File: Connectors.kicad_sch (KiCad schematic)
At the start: 23 parts, among them J1 Precidip 853-87-004-20-001101, J10 Precidip 853-87-004-20-001101, J11 7 pin FPC 0.3mm Aces 51688-00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, J12 Precidip 853-87-004-20-001101, J13 TE 3-2363961-0 receptacle, J15 Precidip 853-87-004-20-001101, J16 TE 3-2363961-0 receptacle, J18 Precidip 852-10-004-20-001101, J2 Precidip 853-87-004-20-001101, J3 7 pin FPC 0.3mm Aces 51688-00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, J4 Precidip 853-87-004-20-001101, J5 7 pin FPC 0.3mm Aces 51688-00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, J6 Precidip 853-87-004-20-001101, J7 Precidip 853-87-004-20-001101, J8 7 pin FPC 0.3mm Aces 51688-00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, J9 Precidip 853-87-004-20-001101

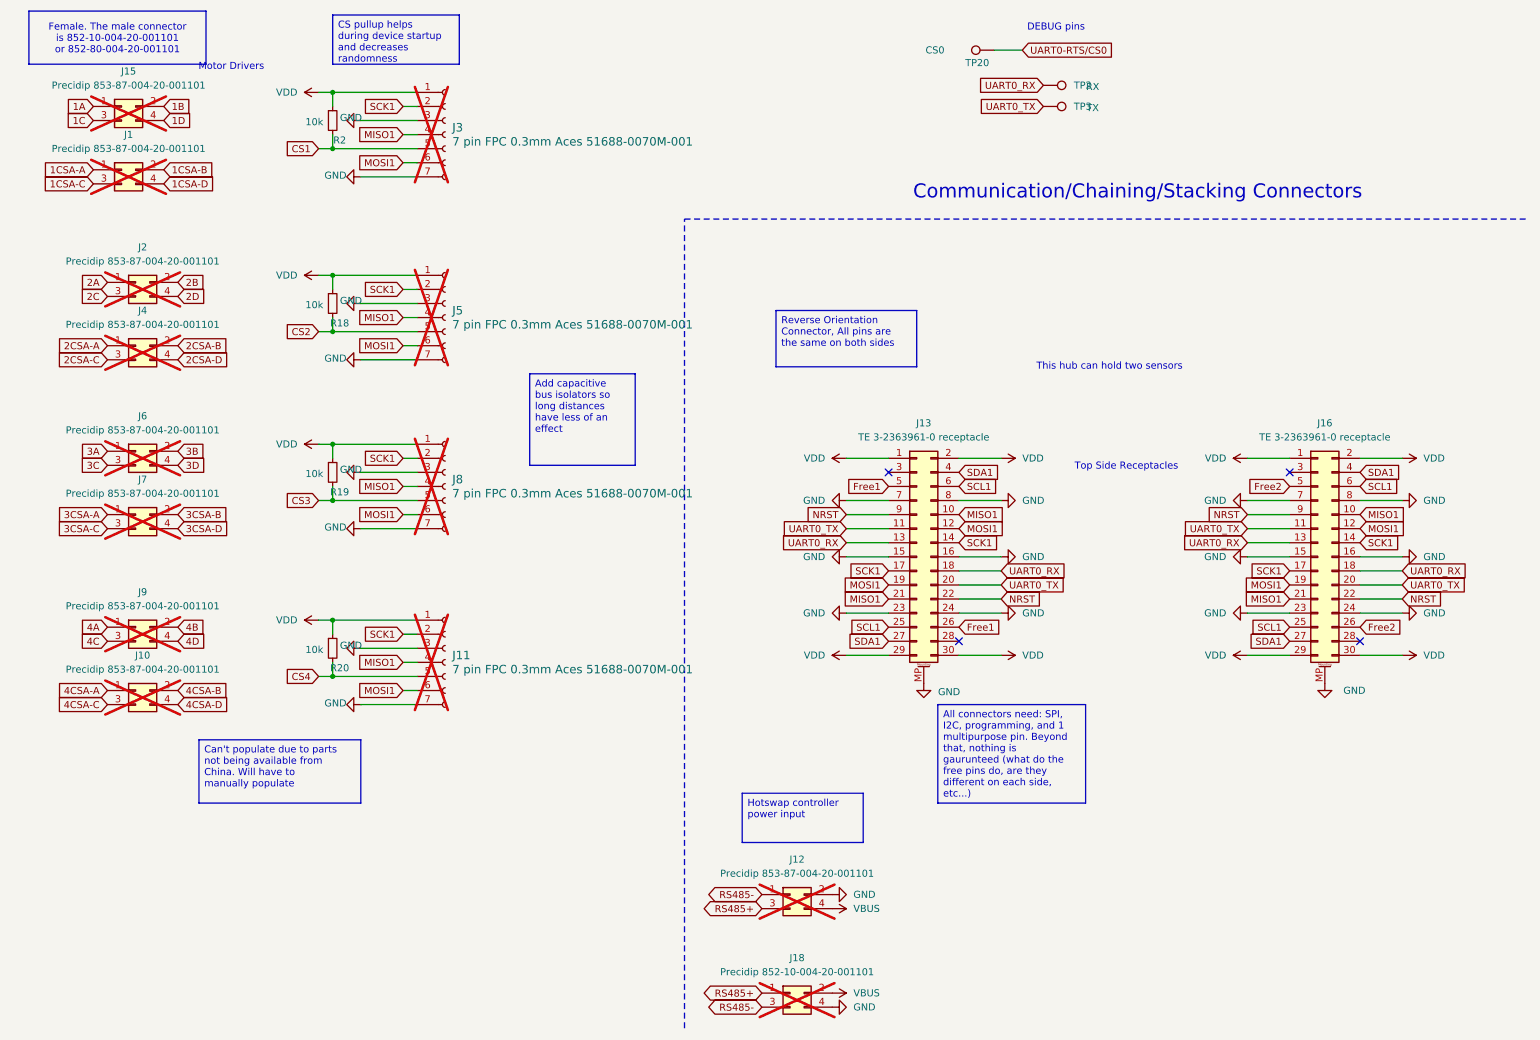
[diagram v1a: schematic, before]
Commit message: Reorganized and made schematic clearer
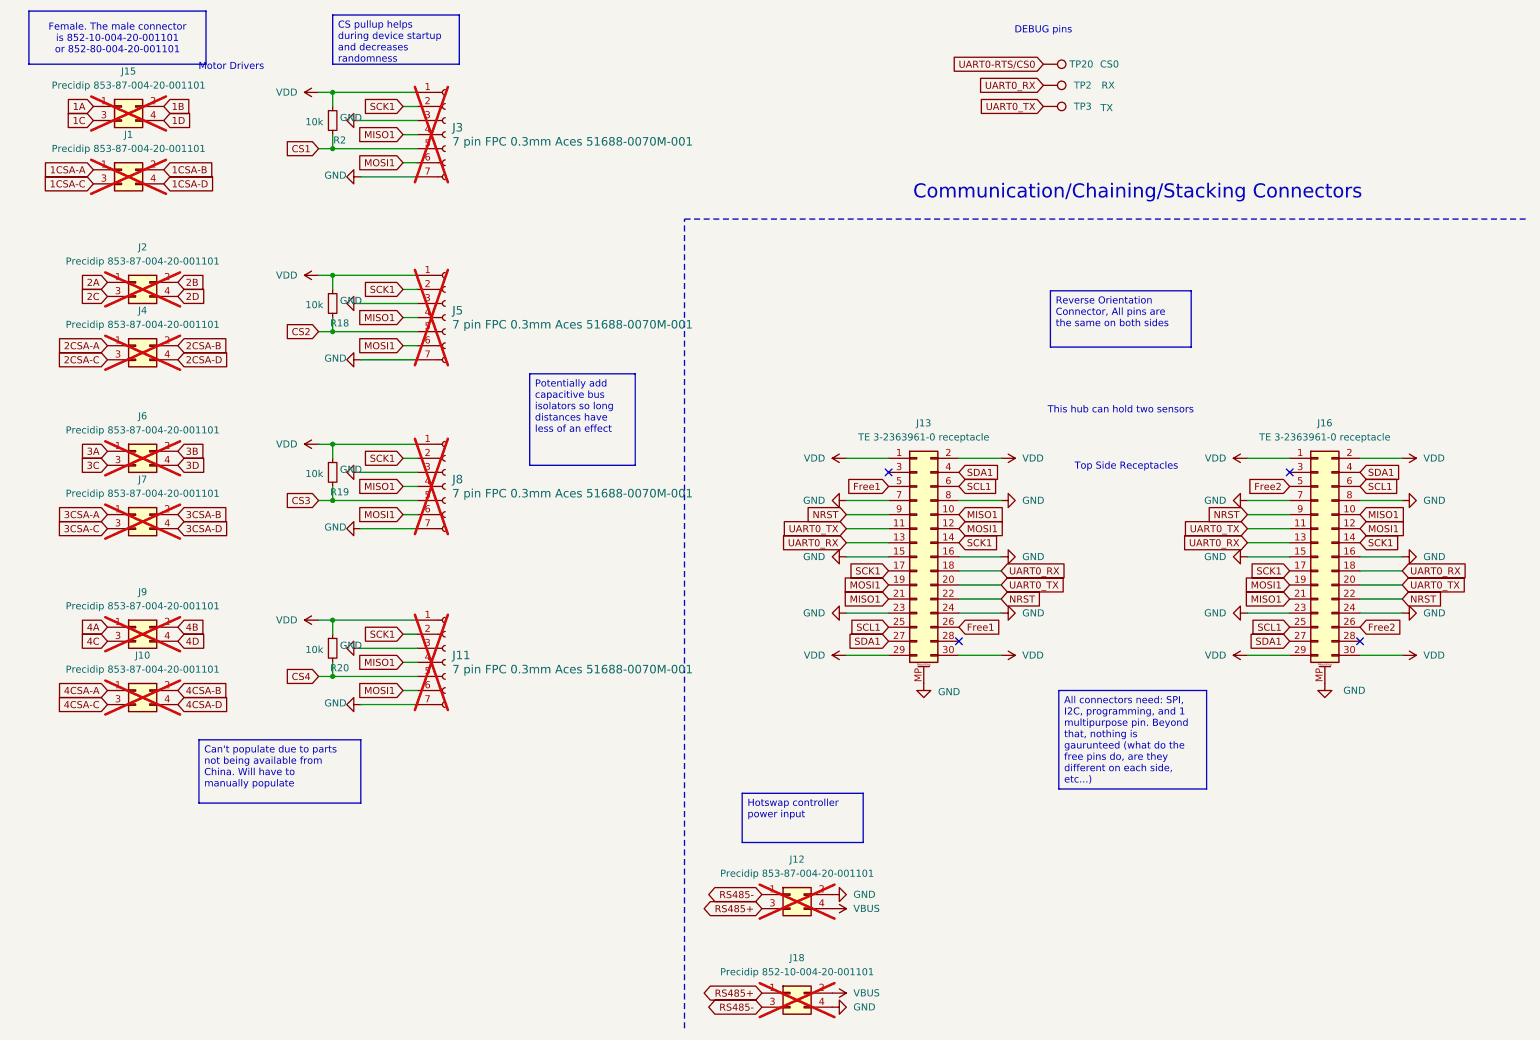
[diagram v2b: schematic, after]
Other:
- moved on the sheet: TP20
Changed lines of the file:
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@@
 	(text "This hub can hold two sensors"
 		(exclude_from_sim no)
-		(at 210.058 78.74 0)
+		(at 212.09 86.614 0)
 		(effects
 			(font
@@
 	(text "DEBUG pins"
 		(exclude_from_sim no)
-		(at 200.406 17.526 0)
+		(at 198.12 18.034 0)
 		(effects
 			(font
@@
 	(text_box "Reverse Orientation Connector, All pins are the same on both sides"
 		(exclude_from_sim no)
-		(at 149.86 68.58 0)
+		(at 199.39 65.024 0)
 		(size 25.4 10.16)
 		(margins 0.9525 0.9525 0.9525 0.9525)
@@
 		)
 	)
-	(text_box "Add capacitive bus isolators so long distances have less of an effect"
+	(text_box "Potentially add capacitive bus isolators so long distances have less of an effect"
 		(exclude_from_sim no)
 		(at 105.41 80.01 0)
@@
 	(text_box "All connectors need: SPI, I2C, programming, and 1 multipurpose pin. Beyond that, nothing is gaurunteed (what do the free pins do, are they different on each side, etc...)\n"
 		(exclude_from_sim no)
-		(at 179.07 139.7 0)
+		(at 200.914 137.16 0)
 		(size 26.67 17.78)
 		(margins 0.9525 0.9525 0.9525 0.9525)
@@
 	(wire
 		(pts
-			(xy 194.31 21.59) (xy 189.23 21.59)
-		)
-		(stroke
-			(width 0)
-			(type default)
-		)
-	)
-	(wire
-		(pts
 			(xy 190.5 130.81) (xy 182.88 130.81)
 		)
@@
 	(global_label "UART0-RTS{slash}CS0"
 		(shape input)
-		(at 194.31 21.59 0)
+		(at 198.12 24.13 180)
 		(fields_autoplaced yes)
 		(effects
@@
 				(size 1.27 1.27)
 			)
-			(justify left)
+			(justify right)
 		)
 		(property "Intersheetrefs" "${INTERSHEET_REFS}"
-			(at 213.2004 21.59 0)
+			(at 179.2296 24.13 0)
 			(effects
 				(font
 					(size 1.27 1.27)
 				)
-				(justify left)
+				(justify right)
 				(hide yes)
 			)
@@
 	(symbol
 		(lib_id "Connector:TestPoint")
-		(at 189.23 21.59 90)
+		(at 198.12 24.13 270)
 		(unit 1)
 		(exclude_from_sim no)
@@
 		(dnp no)
 		(property "Reference" "TP20"
-			(at 186.182 23.876 90)
+			(at 204.978 24.13 90)
 			(effects
 				(font
@@
 		)
 		(property "Value" "CS0"
-			(at 178.562 21.59 90)
+			(at 210.058 24.13 90)
 			(effects
 				(font
@@
 		)
 		(property "Footprint" "TestPoint:TestPoint_Pad_D1.0mm"
-			(at 189.23 16.51 0)
+			(at 198.12 29.21 0)
 			(effects
 				(font
@@
 		)
 		(property "Datasheet" "~"
-			(at 189.23 16.51 0)
+			(at 198.12 29.21 0)
 			(effects
 				(font
@@
 		)
 		(property "Description" "test point"
-			(at 189.23 21.59 0)
+			(at 198.12 24.13 0)
 			(effects
 				(font
@@
 		)
 		(property "Value" "TX"
-			(at 207.01 32.004 90)
+			(at 209.55 32.004 90)
 			(effects
 				(font
@@
 		)
 		(property "Value" "RX"
-			(at 207.01 28.194 90)
+			(at 209.804 27.94 90)
 			(effects
 				(font

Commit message: Improve schematic consistency
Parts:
- J11, J3, J5, J8: value 7 pin FPC 0.3mm Aces 51688-0070M-001 -> FPC 0.3mm Aces 51688-0070M
- TP20: value CS0 -> RTS
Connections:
- net 4CSA-A is gone; now on net ADC-3A: J10.1 (Pin_1)
- net 4CSA-B is gone; now on net ADC-3B: J10.2 (Pin_2)
- net 4CSA-C is gone; now on net ADC-3C: J10.3 (Pin_3)
- net 4CSA-D is gone; now on net ADC-3D: J10.4 (Pin_4)
- net 1A renamed PWM-1A
- net 1B renamed PWM-1B
- net 1C renamed PWM-1C
- net 1CSA-A renamed ADC-1A
- net 1CSA-B renamed ADC-1B
- net 1CSA-C renamed ADC-1C
- net 1CSA-D renamed ADC-1D
- net 1D renamed PWM-1D
- net 2A renamed PWM-2A
- net 2B renamed PWM-2B
- net 2C renamed PWM-2C
- net 2CSA-A renamed ADC-2A
- net 2CSA-B renamed ADC-2B
- net 2CSA-C renamed ADC-2C
- net 2CSA-D renamed ADC-2D
- net 2D renamed PWM-2D
- net 3A renamed PWM-3A
- net 3B renamed PWM-3B
- net 3C renamed PWM-3C
- net 3CSA-A renamed ADC-3A
- net 3CSA-B renamed ADC-3B
- net 3CSA-C renamed ADC-3C
- net 3CSA-D renamed ADC-3D
- net 3D renamed PWM-3D
- net 4A renamed PWM-4A
- net 4B renamed PWM-4B
- net 4C renamed PWM-4C
- net 4D renamed PWM-4D
- net CS1 renamed CS-1
- net CS2 renamed CS-2
- net CS3 renamed CS-3
- net CS4 renamed CS-4
- net Free1 renamed Free-1
- net Free2 renamed Free-2
- net MISO1 renamed MISO
- net MOSI1 renamed MOSI
- net SCK1 renamed SCK
- net SCL1 renamed SCL
- net SDA1 renamed SDA
- net UART0-RTS/CS0 renamed UART0-RTS
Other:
- note added: "Female"
- note added: "Male"
- note removed: "This hub can hold two sensors"
- note removed: "Top Side Receptacles"
- moved on the sheet: J1, J10, J11, J12, J15, J18, J2, J3, J4, J5, J6, J7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

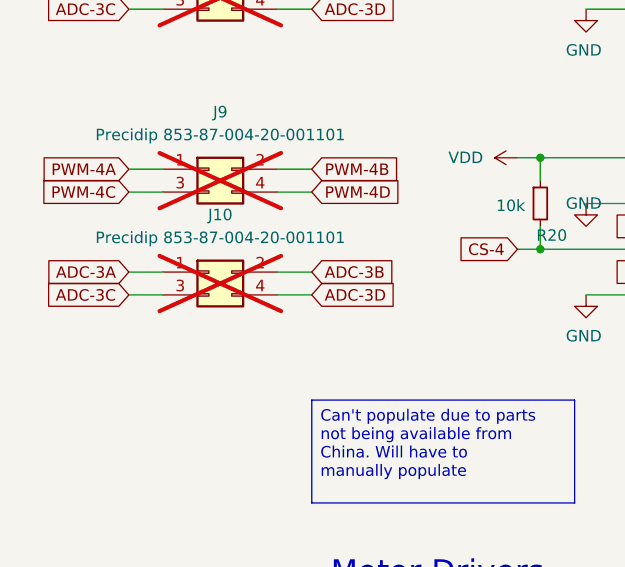
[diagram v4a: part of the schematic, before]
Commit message: Fixed typos with ADC-4 pins, split a few circuits
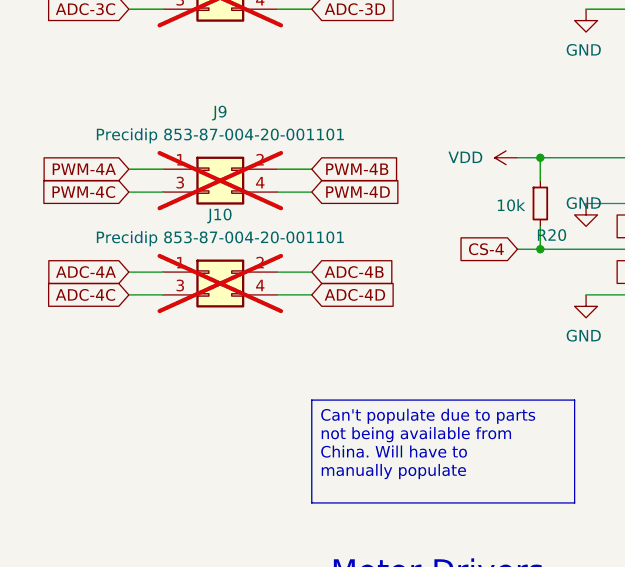
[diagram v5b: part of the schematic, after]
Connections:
- net ADC-3A: no longer J10.1 (Pin_1)
- net ADC-3B: no longer J10.2 (Pin_2)
- net ADC-3C: no longer J10.3 (Pin_3)
- net ADC-3D: no longer J10.4 (Pin_4)
- new net ADC-4A: J10.1 (Pin_1)
- new net ADC-4B: J10.2 (Pin_2)
- new net ADC-4C: J10.3 (Pin_3)
- new net ADC-4D: J10.4 (Pin_4)
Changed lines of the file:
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@@
 		)
 	)
-	(global_label "ADC-3A"
+	(global_label "ADC-4A"
 		(shape input)
 		(at 24.13 158.75 180)
@@
 		)
 	)
-	(global_label "ADC-3C"
+	(global_label "ADC-4C"
 		(shape input)
 		(at 24.13 161.29 180)
@@
 		)
 	)
-	(global_label "ADC-3D"
+	(global_label "ADC-4D"
 		(shape input)
 		(at 44.45 161.29 0)
@@
 		)
 	)
-	(global_label "ADC-3B"
+	(global_label "ADC-4B"
 		(shape input)
 		(at 44.45 158.75 0)

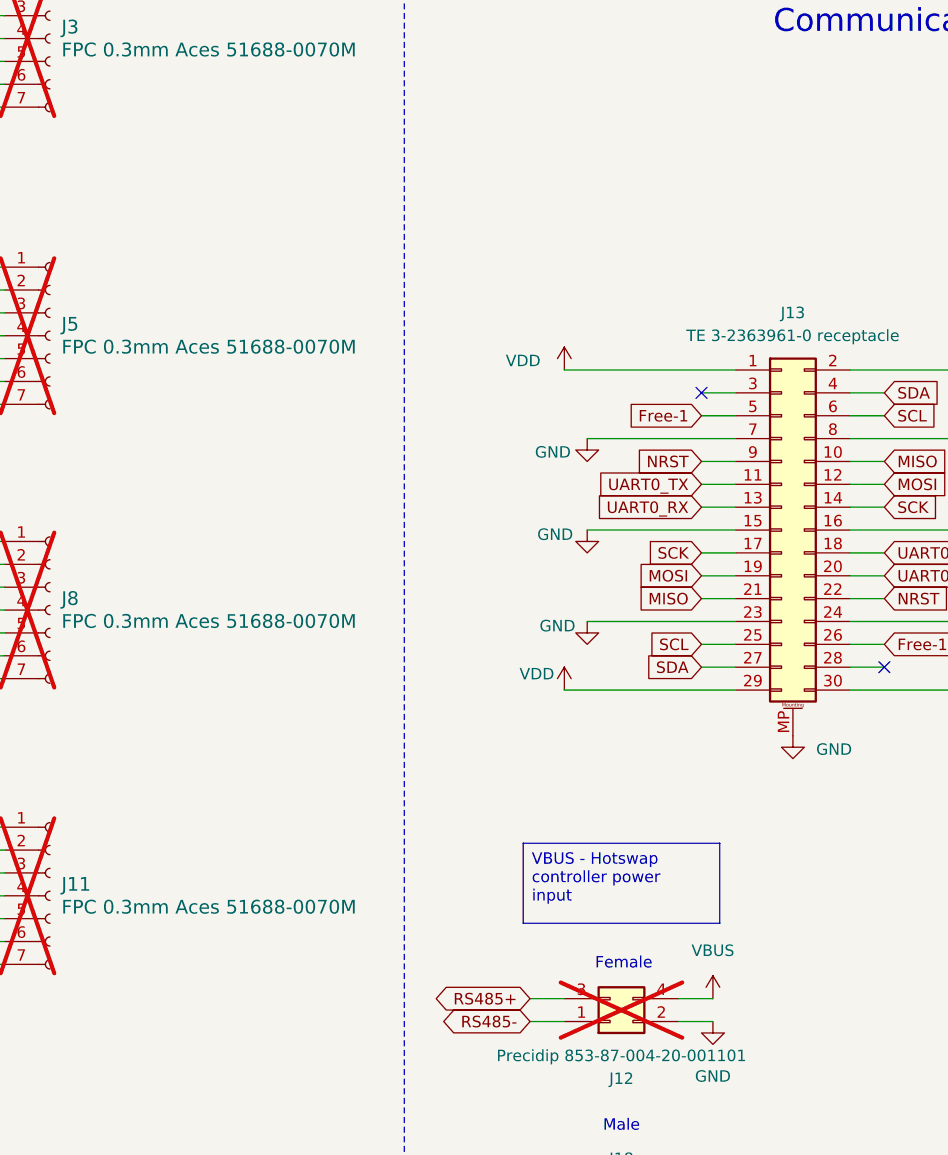
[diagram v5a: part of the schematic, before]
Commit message: Updated potential spec for buffer
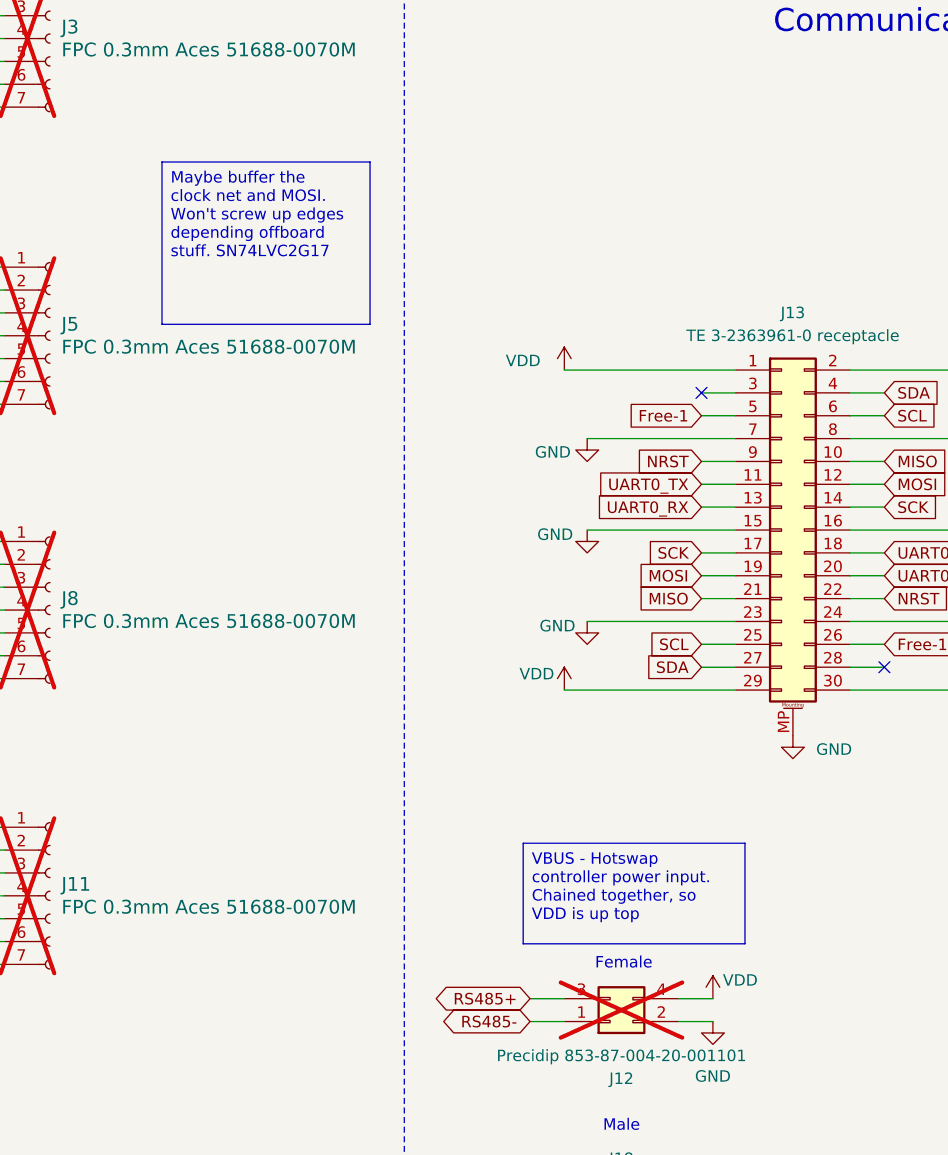
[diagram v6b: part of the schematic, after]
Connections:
- net VBUS: no longer J12.4 (Pin_4)
- net VDD: now also J12.4 (Pin_4)
